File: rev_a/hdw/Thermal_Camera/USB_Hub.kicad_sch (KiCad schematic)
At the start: 22 parts

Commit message: lots of schematic progress
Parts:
- C2501, C2502, C2503, C2504, C2506, C2507: renamed from C?; footprint Capacitors_SMD:C_0603 -> (none); Digi-Key PN 1276-1935-1-ND -> (none); display_footprint 0603 -> (none)
- C2505: renamed from C?; footprint Capacitors_SMD:C_0603 -> (none); Digi-Key PN 399-8153-1-ND -> (none); display_footprint 0603 -> (none)
- C?: footprint Capacitors_SMD:C_0603 -> (none); Digi-Key PN 399-8153-1-ND -> (none); display_footprint 0603 -> (none)
- L2501: renamed from L?; footprint Inductors_SMD:L_0603 -> (none); Digi-Key PN MH1608-601YCT-ND -> (none)
- R2501: renamed from R?; footprint Resistors_SMD:R_0603 -> (none); Digi-Key PN 541-2982-1-ND -> (none); Wattage 1/10W -> (none); display_footprint 0603 -> (none)
- R2502, R2503, R2504, R2505, R2506, R2507: renamed from R?; footprint Resistors_SMD:R_0603 -> (none); Digi-Key PN 541-10.0KHCT-ND -> (none); Wattage 1/10W -> (none); display_footprint 0603 -> (none)
- gave numbers to parts that had none: 6

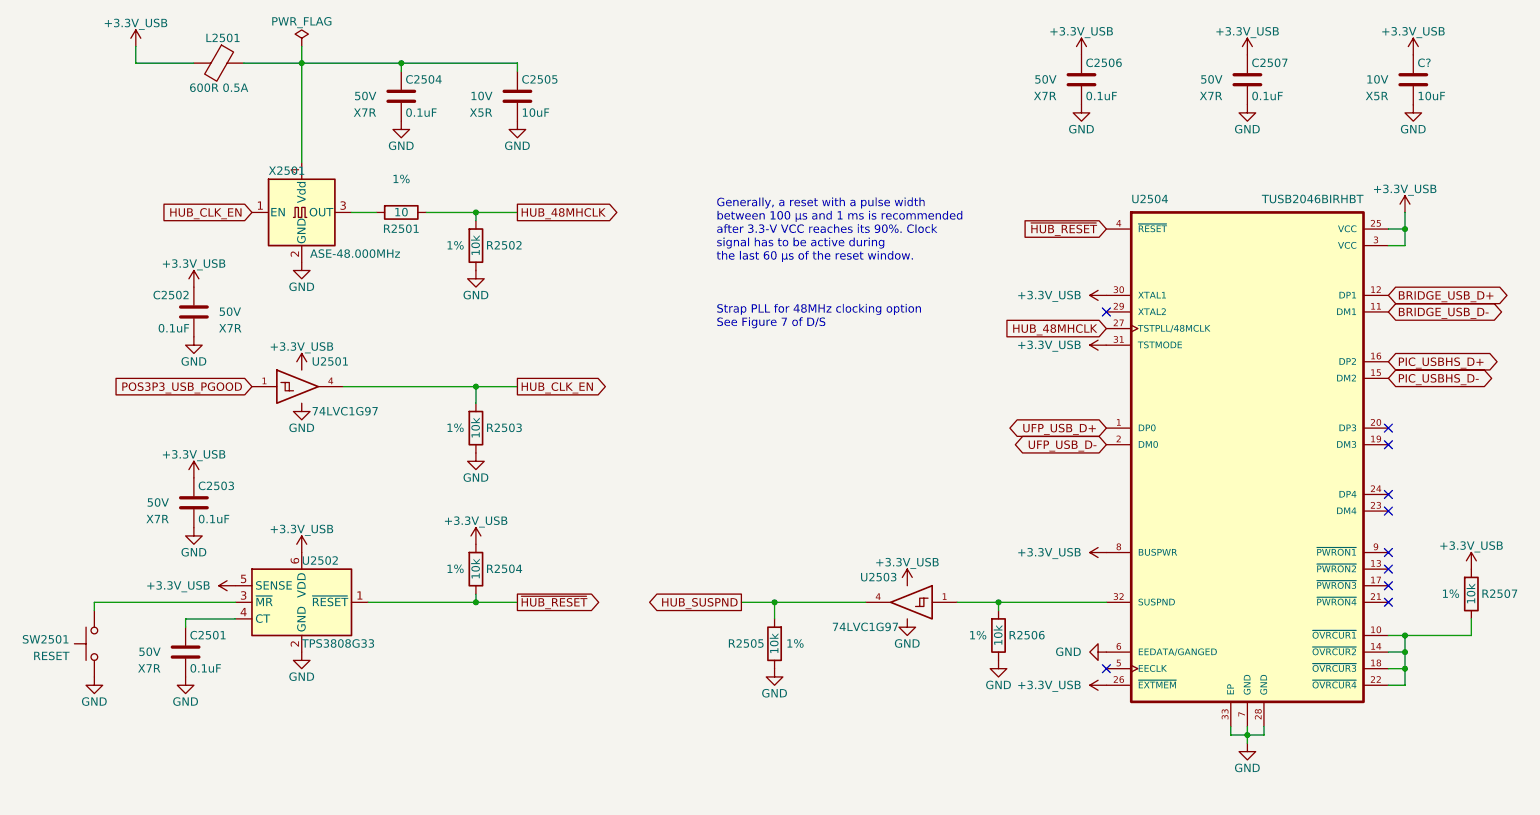
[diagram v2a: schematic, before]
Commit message: assigned a ton of footprints
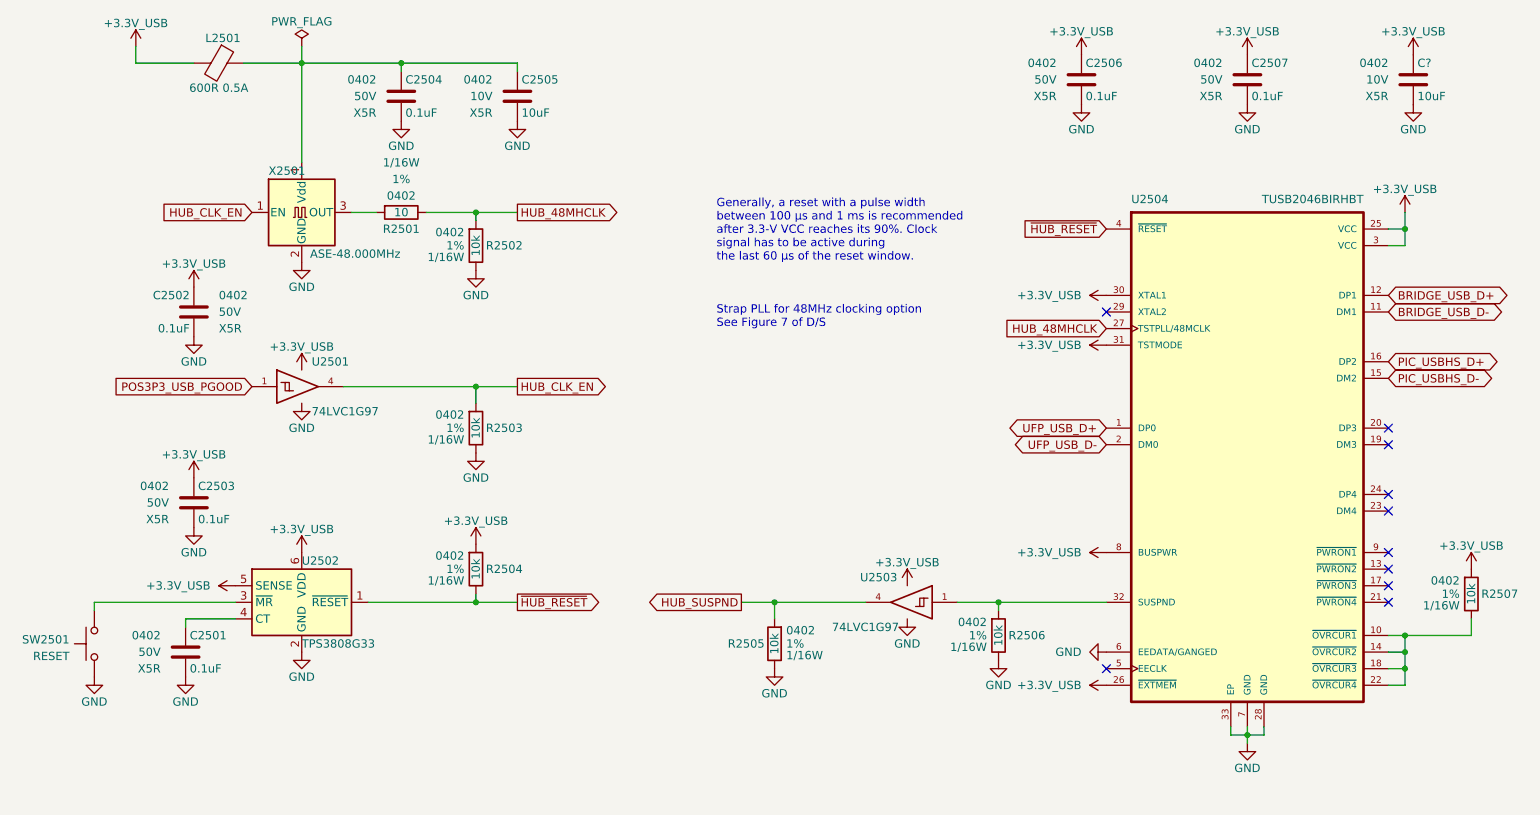
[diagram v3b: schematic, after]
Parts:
- C2501, C2502, C2503, C2504, C2506, C2507: footprint (none) -> Capacitors_SMD:C_0402; Dielectric X7R -> X5R; display_footprint (none) -> 0402
- C2505, C?: footprint (none) -> Capacitors_SMD:C_0402; display_footprint (none) -> 0402
- L2501: footprint (none) -> Inductors_SMD:L_0402
- R2501, R2502, R2503, R2504, R2505, R2506, R2507: footprint (none) -> Resistors_SMD:R_0402; Wattage (none) -> 1/16W; display_footprint (none) -> 0402
- U2501, U2503: Digi-Key PN 1727-1772-1-ND -> 296-15582-1-ND
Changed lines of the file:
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@@
 			)
 		)
-		(property "Footprint" ""
+		(property "Footprint" "Capacitors_SMD:C_0402"
 			(at 39.0652 115.57 0)
 			(effects
@@
 			)
 		)
-		(property "display_footprint" ""
+		(property "display_footprint" "0402"
 			(at 34.29 109.22 0)
 			(effects
@@
 			)
 		)
-		(property "Dielectric" "X7R"
+		(property "Dielectric" "X5R"
 			(at 34.29 114.3 0)
 			(effects
@@
 			)
 		)
-		(property "Footprint" ""
+		(property "Footprint" "Capacitors_SMD:C_0402"
 			(at 40.3352 92.71 0)
 			(effects
@@
 			)
 		)
-		(property "display_footprint" ""
+		(property "display_footprint" "0402"
 			(at 35.56 86.36 0)
 			(effects
@@
 			)
 		)
-		(property "Dielectric" "X7R"
+		(property "Dielectric" "X5R"
 			(at 35.56 91.44 0)
 			(effects
@@
 			)
 		)
-		(property "Footprint" ""
+		(property "Footprint" "Capacitors_SMD:C_0402"
 			(at 176.2252 27.94 0)
 			(effects
@@
 			)
 		)
-		(property "display_footprint" ""
+		(property "display_footprint" "0402"
 			(at 171.45 21.59 0)
 			(effects
@@
 			)
 		)
-		(property "Dielectric" "X7R"
+		(property "Dielectric" "X5R"
 			(at 171.45 26.67 0)
 			(effects
@@
 			)
 		)
-		(property "Footprint" ""
+		(property "Footprint" "Resistors_SMD:R_0402"
 			(at 82.55 99.06 0)
 			(effects
@@
 			)
 		)
-		(property "display_footprint" ""
+		(property "display_footprint" "0402"
 			(at 80.772 97.028 0)
 			(effects
@@
 			)
 		)
-		(property "Wattage" ""
+		(property "Wattage" "1/16W"
 			(at 80.772 100.838 0)
 			(effects
@@
 			)
 		)
-		(property "Footprint" ""
+		(property "Footprint" "Resistors_SMD:R_0402"
 			(at 162.56 109.22 0)
 			(effects
@@
 			)
 		)
-		(property "display_footprint" ""
+		(property "display_footprint" "0402"
 			(at 160.782 107.188 0)
 			(effects
@@
 			)
 		)
-		(property "Wattage" ""
+		(property "Wattage" "1/16W"
 			(at 160.782 110.998 0)
 			(effects
@@
 			)
 		)
-		(property "Footprint" ""
+		(property "Footprint" "Capacitors_SMD:C_0402"
 			(at 201.6252 27.94 0)
 			(effects
@@
 			)
 		)
-		(property "display_footprint" ""
+		(property "display_footprint" "0402"
 			(at 196.85 21.59 0)
 			(effects
@@
 			)
 		)
-		(property "Dielectric" "X7R"
+		(property "Dielectric" "X5R"
 			(at 196.85 26.67 0)
 			(effects
@@
 			)
 		)
-		(property "Footprint" ""
+		(property "Footprint" "Inductors_SMD:L_0402"
 			(at 43.18 19.812 90)
 			(effects
@@
 			)
 		)
-		(property "Footprint" ""
+		(property "Footprint" "Resistors_SMD:R_0402"
 			(at 128.27 110.49 0)
 			(effects
@@
 			)
 		)
-		(property "display_footprint" ""
+		(property "display_footprint" "0402"
 			(at 130.048 108.458 0)
 			(effects
@@
 			)
 		)
-		(property "Wattage" ""
+		(property "Wattage" "1/16W"
 			(at 130.048 112.268 0)
 			(effects
@@
 			)
 		)
-		(property "Footprint" ""
+		(property "Footprint" "Resistors_SMD:R_0402"
 			(at 71.12 44.45 0)
 			(effects
@@
 			)
 		)
-		(property "display_footprint" ""
+		(property "display_footprint" "0402"
 			(at 71.12 41.91 90)
 			(effects
@@
 			)
 		)
-		(property "Wattage" ""
+		(property "Wattage" "1/16W"
 			(at 71.12 36.83 90)
 			(effects
@@
 			)
 		)
-		(property "Footprint" ""
+		(property "Footprint" "Capacitors_SMD:C_0402"
 			(at 227.0252 27.94 0)
 			(effects
@@
 			)
 		)
-		(property "display_footprint" ""
+		(property "display_footprint" "0402"
 			(at 222.25 21.59 0)
 			(effects
@@
 			)
 		)
-		(property "Footprint" ""
+		(property "Footprint" "Resistors_SMD:R_0402"
 			(at 82.55 49.53 0)
 			(effects
@@
 			)
 		)
-		(property "display_footprint" ""
+		(property "display_footprint" "0402"
 			(at 80.772 47.498 0)
 			(effects
@@
 			)
 		)
-		(property "Wattage" ""
+		(property "Wattage" "1/16W"
 			(at 80.772 51.308 0)
 			(effects
@@
 			)
 		)
-		(property "Footprint" ""
+		(property "Footprint" "Capacitors_SMD:C_0402"
 			(at 38.4048 63.5 0)
 			(effects
@@
 			)
 		)
-		(property "display_footprint" ""
+		(property "display_footprint" "0402"
 			(at 43.18 57.15 0)
 			(effects
@@
 			)
 		)
-		(property "Dielectric" "X7R"
+		(property "Dielectric" "X5R"
 			(at 43.18 62.23 0)
 			(effects
@@
 			)
 		)
-		(property "Footprint" ""
+		(property "Footprint" "Capacitors_SMD:C_0402"
 			(at 89.8652 30.48 0)
 			(effects
@@
 			)
 		)
-		(property "display_footprint" ""
+		(property "display_footprint" "0402"
 			(at 85.09 24.13 0)
 			(effects
@@
 			)
 		)
-		(property "Digi-Key PN" "1727-1772-1-ND"
+		(property "Digi-Key PN" "296-15582-1-ND"
 			(at 148.59 104.14 0)
 			(effects
@@
 			)
 		)
-		(property "Digi-Key PN" "1727-1772-1-ND"
+		(property "Digi-Key PN" "296-15582-1-ND"
 			(at 55.88 71.12 0)
 			(effects
@@
 			)
 		)
-		(property "Footprint" ""
+		(property "Footprint" "Capacitors_SMD:C_0402"
 			(at 72.0852 30.48 0)
 			(effects
@@
 			)
 		)
-		(property "display_footprint" ""
+		(property "display_footprint" "0402"
 			(at 67.31 24.13 0)
 			(effects
@@
 			)
 		)
-		(property "Dielectric" "X7R"
+		(property "Dielectric" "X5R"
 			(at 67.31 29.21 0)
 			(effects
@@
 			)
 		)
-		(property "Footprint" ""
+		(property "Footprint" "Resistors_SMD:R_0402"
 			(at 82.55 77.47 0)
 			(effects
@@
 			)
 		)
-		(property "display_footprint" ""
+		(property "display_footprint" "0402"
 			(at 80.772 75.438 0)
 			(effects
@@
 			)
 		)
-		(property "Wattage" ""
+		(property "Wattage" "1/16W"
 			(at 80.772 79.248 0)
 			(effects
@@
 			)
 		)
-		(property "Footprint" ""
+		(property "Footprint" "Resistors_SMD:R_0402"
 			(at 234.95 102.87 0)
 			(effects
@@
 			)
 		)
-		(property "display_footprint" ""
+		(property "display_footprint" "0402"
 			(at 233.172 100.838 0)
 			(effects
@@
 			)
 		)
-		(property "Wattage" ""
+		(property "Wattage" "1/16W"
 			(at 233.172 104.648 0)
 			(effects

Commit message: assigned some part numbers
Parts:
- C2501, C2502, C2503, C2504, C2506, C2507: Digi-Key PN (none) -> 490-10697-1-ND
- C2505, C?: Digi-Key PN (none) -> 490-GRM155R61A106ME11DCT-ND
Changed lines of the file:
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@@
 			)
 		)
-		(property "Digi-Key PN" ""
+		(property "Digi-Key PN" "490-10697-1-ND"
 			(at 48.895 99.06 0)
 			(effects
@@
 			)
 		)
-		(property "Digi-Key PN" ""
+		(property "Digi-Key PN" "490-10697-1-ND"
 			(at 50.165 76.2 0)
 			(effects
@@
 			)
 		)
-		(property "Digi-Key PN" ""
+		(property "Digi-Key PN" "490-10697-1-ND"
 			(at 186.055 11.43 0)
 			(effects
@@
 			)
 		)
-		(property "Digi-Key PN" ""
+		(property "Digi-Key PN" "490-10697-1-ND"
 			(at 211.455 11.43 0)
 			(effects
@@
 			)
 		)
-		(property "Digi-Key PN" ""
+		(property "Digi-Key PN" "490-GRM155R61A106ME11DCT-ND"
 			(at 226.06 24.13 0)
 			(effects
@@
 			)
 		)
-		(property "Digi-Key PN" ""
+		(property "Digi-Key PN" "490-10697-1-ND"
 			(at 28.575 46.99 0)
 			(effects
@@
 			)
 		)
-		(property "Digi-Key PN" ""
+		(property "Digi-Key PN" "490-GRM155R61A106ME11DCT-ND"
 			(at 88.9 26.67 0)
 			(effects
@@
 			)
 		)
-		(property "Digi-Key PN" ""
+		(property "Digi-Key PN" "490-10697-1-ND"
 			(at -28.194 201.422 0)
 			(effects

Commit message: assigned resistor part numbers
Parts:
- R2501: Digi-Key PN (none) -> RMCF0402FT10R0CT-ND
- R2502, R2503, R2504, R2505, R2506, R2507: Digi-Key PN (none) -> RMCF0402FT10K0CT-ND
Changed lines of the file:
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@@
 			)
 		)
-		(property "Digi-Key PN" ""
+		(property "Digi-Key PN" "RMCF0402FT10K0CT-ND"
 			(at 82.55 99.06 0)
 			(effects
@@
 			)
 		)
-		(property "Digi-Key PN" ""
+		(property "Digi-Key PN" "RMCF0402FT10K0CT-ND"
 			(at 162.56 109.22 0)
 			(effects
@@
 			)
 		)
-		(property "Digi-Key PN" ""
+		(property "Digi-Key PN" "RMCF0402FT10K0CT-ND"
 			(at 128.27 110.49 0)
 			(effects
@@
 			)
 		)
-		(property "Digi-Key PN" ""
+		(property "Digi-Key PN" "RMCF0402FT10R0CT-ND"
 			(at 60.96 36.83 0)
 			(effects
@@
 			)
 		)
-		(property "Digi-Key PN" ""
+		(property "Digi-Key PN" "RMCF0402FT10K0CT-ND"
 			(at 82.55 49.53 0)
 			(effects
@@
 			)
 		)
-		(property "Digi-Key PN" ""
+		(property "Digi-Key PN" "RMCF0402FT10K0CT-ND"
 			(at 82.55 77.47 0)
 			(effects
@@
 			)
 		)
-		(property "Digi-Key PN" ""
+		(property "Digi-Key PN" "RMCF0402FT10K0CT-ND"
 			(at 234.95 102.87 0)
 			(effects

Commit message: lots of PCB placement progress
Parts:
- added C2509: 0.1uF, Capacitors_SMD:C_0402, symbol Custom_Library:C_Custom
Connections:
- net +3.3V_USB: now also C2509.1
- net GND: now also C2509.2
- net HUB_48MHCLK: no longer R2502.1
- net at R2501.1, X2501.3 (OUT): now also R2502.1
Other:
- moved on the sheet: R2501, R2502
